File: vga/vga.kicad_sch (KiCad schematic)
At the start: 28 parts, among them IC1 Jungle TDA9385, J1 VGA, J2 TV Interface, Q1 BC847BDW1, U1 SN74LS86ADR, U2 Pico

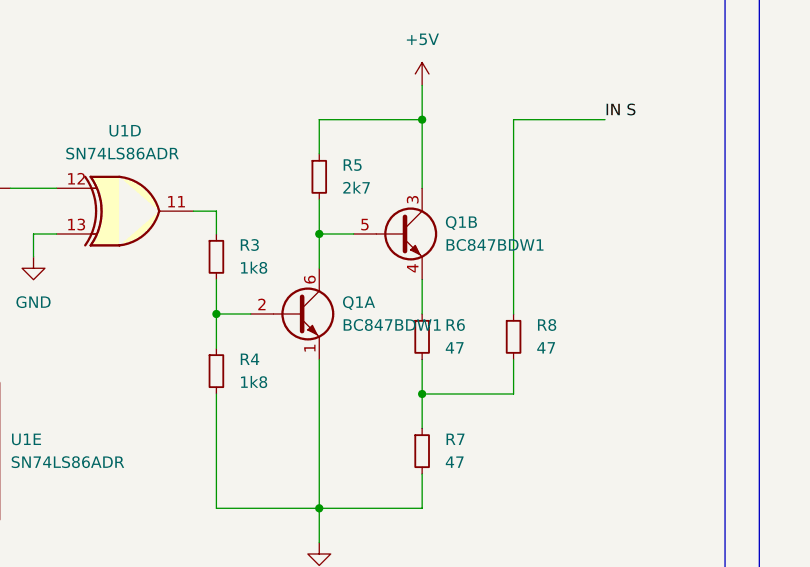
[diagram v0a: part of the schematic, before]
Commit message: fix incorrect footprint in vga board; rewrite stick codebase to use pcf8575 i/o expanders and vga codebase to fix bugs and support rgb blanking
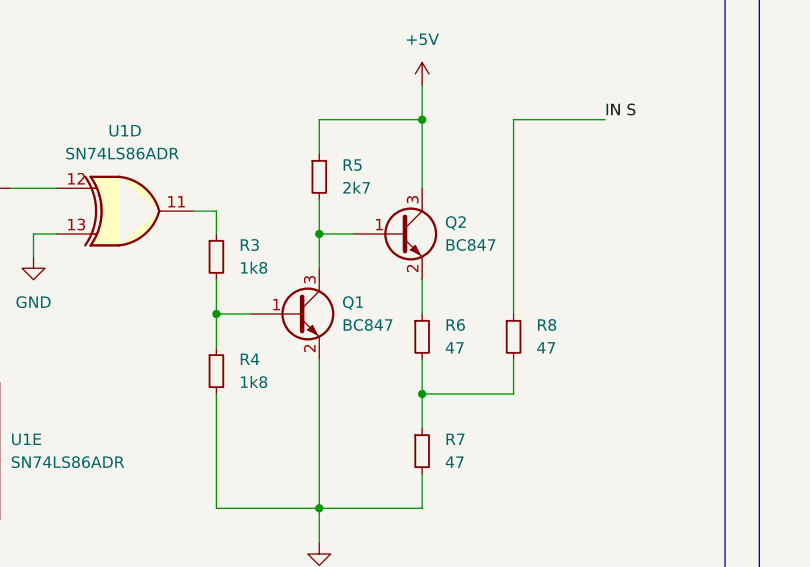
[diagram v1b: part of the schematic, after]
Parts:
- removed Q1: BC847BDW1, Package_TO_SOT_SMD:SOT-363_SC-70-6, symbol Transistor_BJT:BC847BDW1
- added Q1, Q2: BC847, Package_TO_SOT_SMD:SOT-23, symbol Transistor_BJT:BC847
- U1: footprint Package_SO:SOIC-14-16_3.9x9.9mm_P1.27mm -> Package_SO:SOIC-14_3.9x8.7mm_P1.27mm
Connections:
- net +5V: now also Q2.3 (C)
- net GND: now also Q1.2 (E)
- net at R6.1: now also Q2.2 (E)
- net at R5.2: now also Q1.3 (C), Q2.1 (B)
- net at R3.2, R4.1: now also Q1.1 (B)
